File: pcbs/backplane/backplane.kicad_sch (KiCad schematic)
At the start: 65 parts

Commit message: Schematic file fix, misc. PCB
Fixed issue with KiCAD's automatic V5→V6 migration (corrected in 6.0.11) that caused problems with component references in multi-channel schematic sheets
Finished migration in amp ctrl PCB, inc. re-assigning "exclude from BOM" attributes to testpoints, solder jumpers
Added mounting hole to amp ctrl PCB for addl support to Ethernet jacks, power connector through stiffener
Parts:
- C10, C2, C20, C3, C61, C62: renamed from ?; value 100nF 50V X7R -> (none); footprint Capacitor_SMD:C_0603_1608Metric -> (none)
- C16, C17, C18, C19: renamed from ?; value 1uF 50V X7R -> (none); footprint Capacitor_SMD:C_0805_2012Metric -> (none)
- J10, J11, J9: renamed from ?; value AFBR-2624Z -> (none); footprint Martinos:AFBR-xx2xZ -> (none)
- J12: renamed from ?; value AFBR-1624Z -> (none); footprint Martinos:AFBR-xx2xZ -> (none)
- J17, J22, J27, J32, J37, J42, J47, J8: renamed from ?; value Conn_01x02 -> (none); footprint Martinos:Connector_Phoenix_1792229 -> (none)
- R10, R11, R3, R4: renamed from ?; value 1 -> (none); footprint Resistor_SMD:R_0805_2012Metric -> (none)
- R12: renamed from ?; value 560 -> (none); footprint Resistor_SMD:R_0805_2012Metric -> (none)
- R5: renamed from ?; value 10 0.25W -> (none); footprint Resistor_SMD:R_2010_5025Metric -> (none)
- R6, R7: renamed from ?; value 1 -> (none); footprint Resistor_SMD:R_1206_3216Metric -> (none)
- R8: renamed from ?; value 15K -> (none); footprint Resistor_SMD:R_0805_2012Metric -> (none)
- R9: renamed from ?; value 1K -> (none); footprint Resistor_SMD:R_0805_2012Metric -> (none)
- TP1, TP2, TP3, TP5: renamed from ?; value TestPoint_Flag -> (none); footprint TestPoint:TestPoint_Keystone_5019_Minature -> (none)
- gave numbers to parts that had none: 29

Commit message: Amp ctrl: lengthened ADC & DAC reset delay to ~50 ms (#14) Backplane: added clock multiplier for 10 Mhz scanner clock (fixes #21) Backplane: reduced R5 from 10 to 1 ohm, to avoid excessive voltage drop (#20) Backplane: replaced 15V regulator with efficient voltage limiter (#20) Backplane: changed all mounting holes to signal ground Backplane: replaced +2.5V regulator with a higher-current model to support FPGA I/O bank current draw Updated to KiCAD 8
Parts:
- C10, C2, C20, C3, C61, C62: value (none) -> 100nF 50V X7R; footprint (none) -> Capacitor_SMD:C_0603_1608Metric
- C16, C17, C18, C19: value (none) -> 1uF 50V X7R; footprint (none) -> Capacitor_SMD:C_0805_2012Metric
- J10, J11, J9: value (none) -> AFBR-2624Z; footprint (none) -> Martinos:AFBR-xx2xZ
- J12: value (none) -> AFBR-1624Z; footprint (none) -> Martinos:AFBR-xx2xZ
- J17, J22, J27, J32, J37, J42, J47, J8: value (none) -> Conn_01x02; footprint (none) -> Martinos:Connector_Phoenix_1792229
- R10, R11, R3, R4: value (none) -> 1; footprint (none) -> Resistor_SMD:R_0805_2012Metric
- R12: value (none) -> 560; footprint (none) -> Resistor_SMD:R_0805_2012Metric
- R5: value (none) -> 1 0.25W; footprint (none) -> Resistor_SMD:R_2010_5025Metric; Part Number RK73H2HTTE10R0F -> RK73H2HTTE1R00F
- R6, R7: value (none) -> 1; footprint (none) -> Resistor_SMD:R_1206_3216Metric
- R8: value (none) -> 15K; footprint (none) -> Resistor_SMD:R_0805_2012Metric
- R9: value (none) -> 1K; footprint (none) -> Resistor_SMD:R_0805_2012Metric
- TP1, TP2, TP3, TP5: value (none) -> TestPoint_Flag; footprint (none) -> TestPoint:TestPoint_Keystone_5019_Minature
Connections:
- net GND: now also H11.1, H14.1, H16.1, H17.1, H18.1, H19.1, H20.1, H5.1, H7.1, H9.1
- net GNDPWR: no longer H11.1, H14.1, H16.1, H17.1, H18.1, H19.1, H20.1, H5.1, H7.1, H9.1

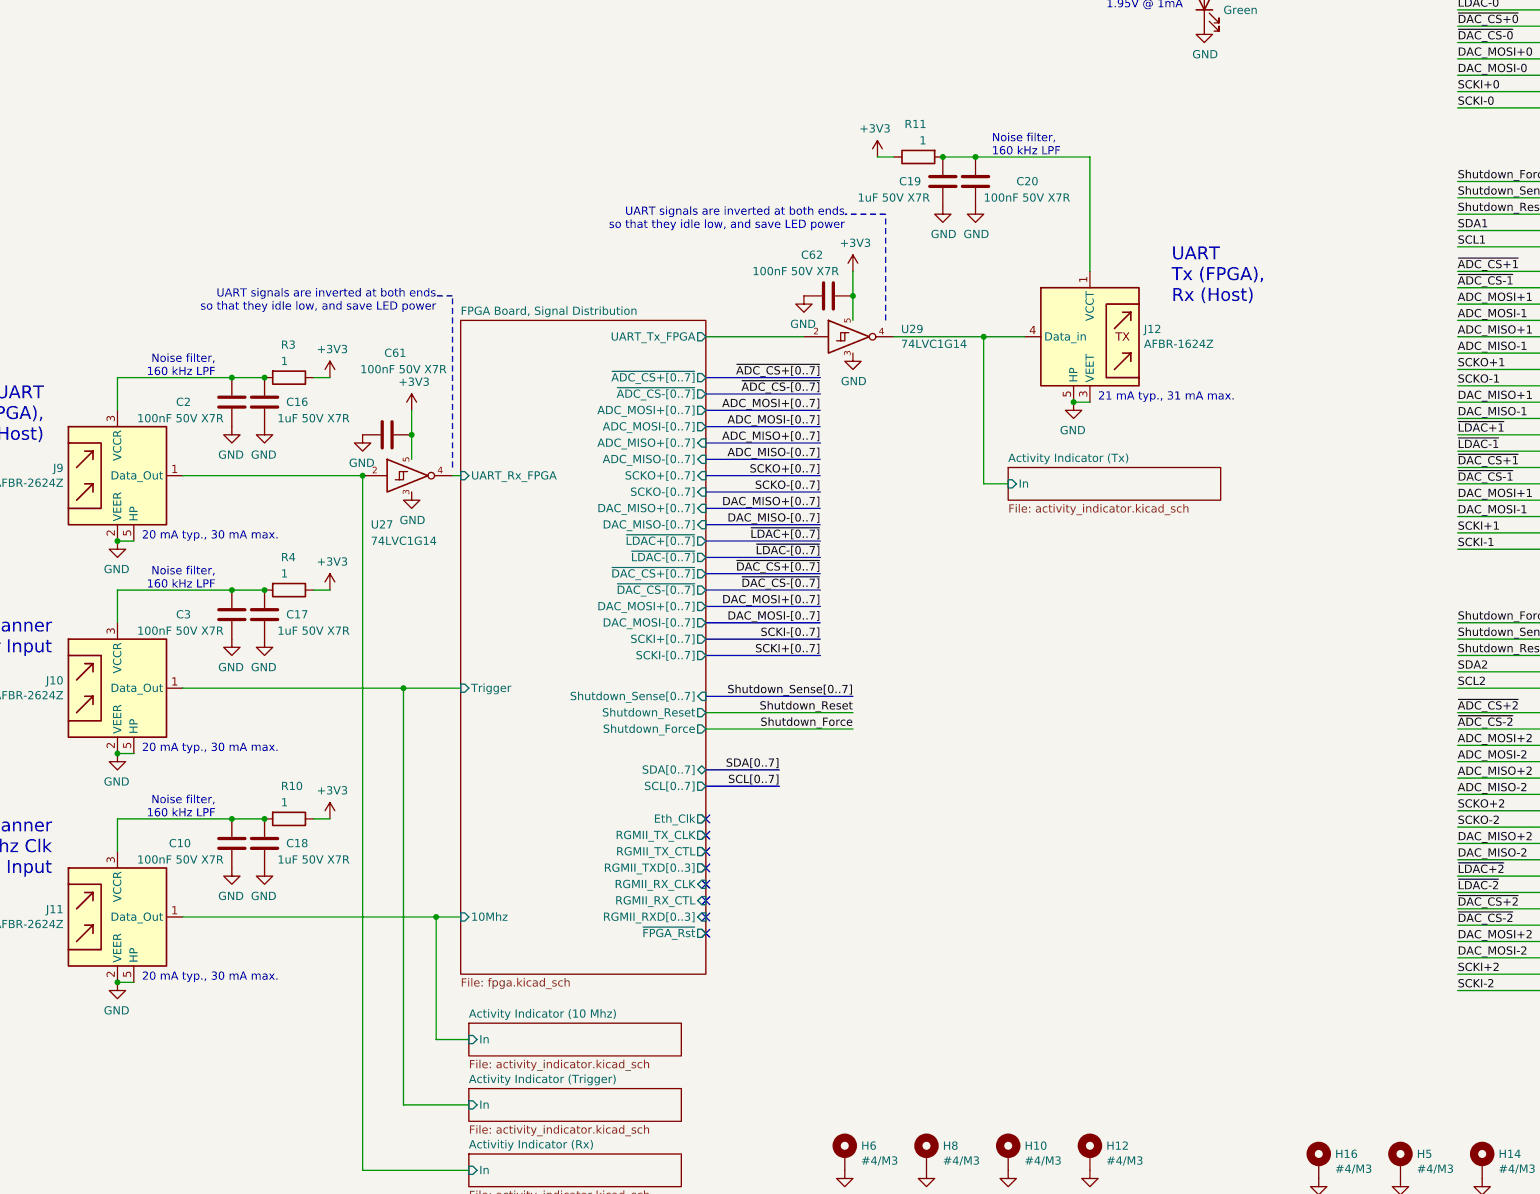
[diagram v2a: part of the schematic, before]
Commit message: Comms fix, misc. improvements
Added 33KΩ pull-ups & pull-downs to amp ctrl board's LVDS inputs, to solve issues caused by unconfigured FPGA pins during boot (fixes #23)
Swapped backplane power input polarity for consistency with power connectors (fixes #20)
Added "manual enable" optical input to backplane, for safety: requires positive enable to keep amplifiers enabled
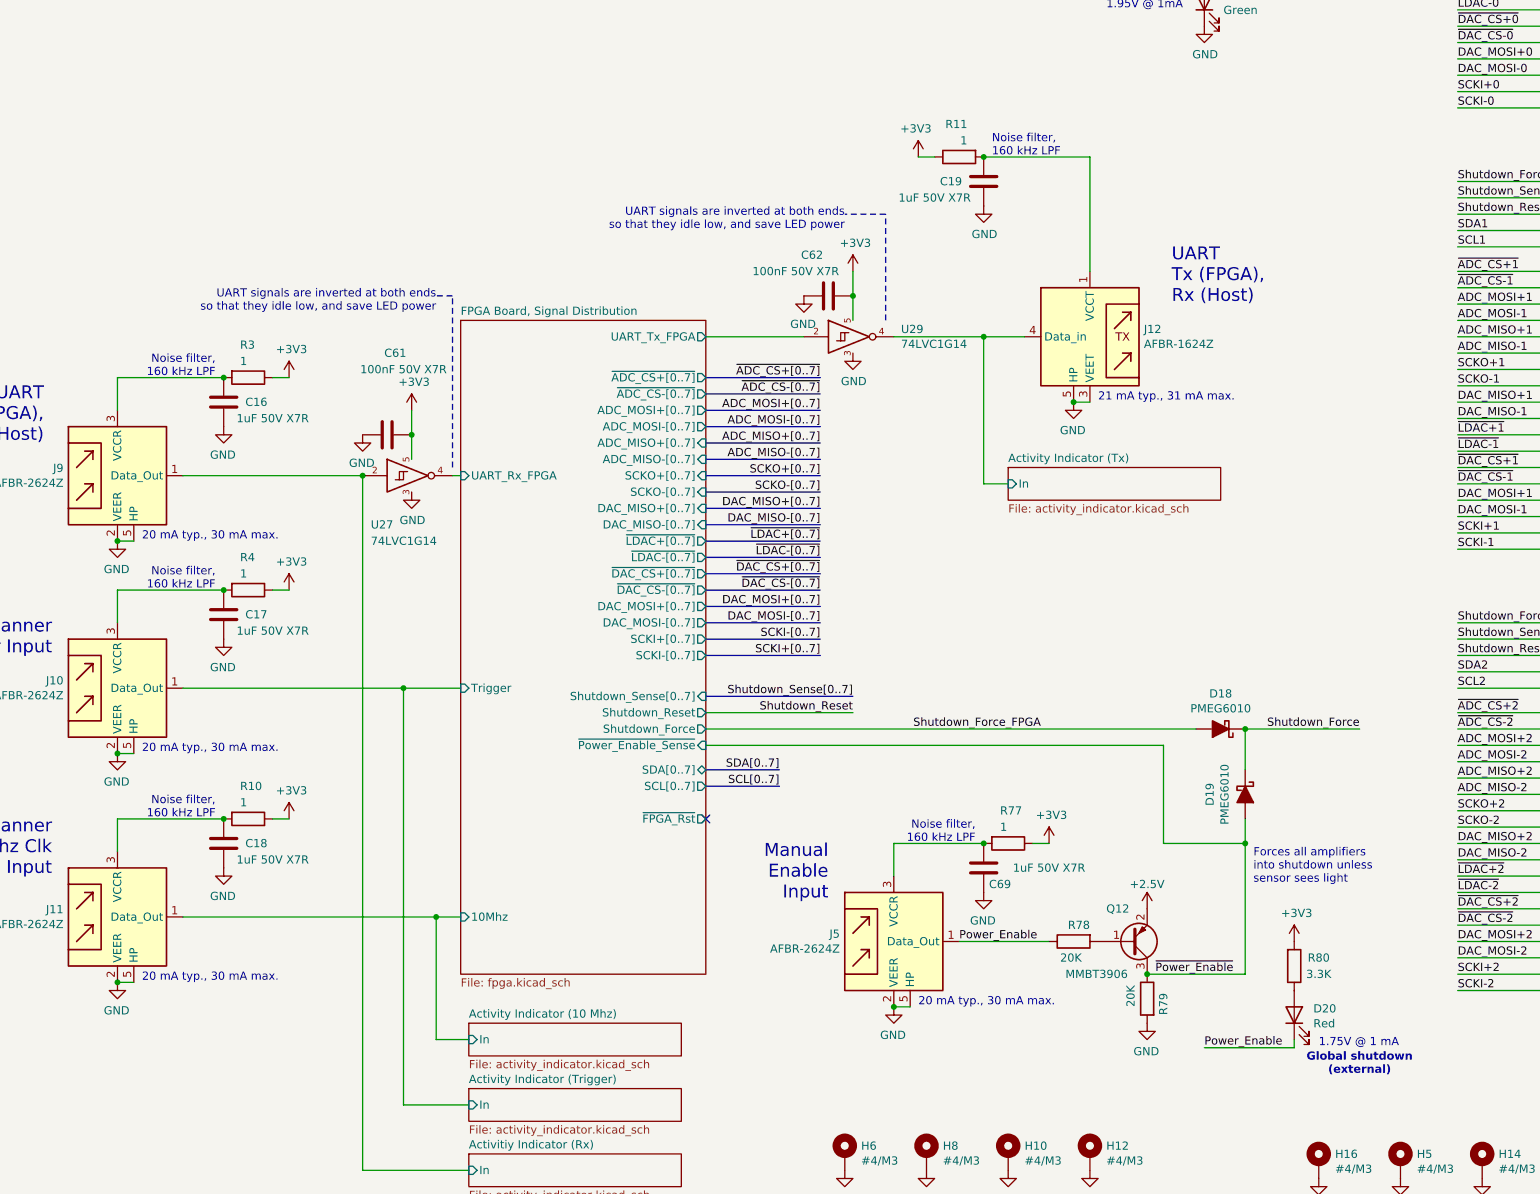
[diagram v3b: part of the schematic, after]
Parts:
- removed C10, C2, C20, C3: 100nF 50V X7R, Capacitor_SMD:C_0603_1608Metric, symbol Device:C
- added C69: 1uF 50V X7R, Capacitor_SMD:C_0805_2012Metric, symbol Device:C
- added D18, D19: PMEG6010, Diode_SMD:D_SOD-123F, symbol backplane-rescue:D_Schottky_ALT-Device
- added D20: Red, LED_SMD:LED_0805_2012Metric, symbol Device:LED
- added J5: AFBR-2624Z, Don:AFBR-xx2xZ, symbol Fiber_Optic:AFBR-2624Z
- added Q12: MMBT3906, Package_TO_SOT_SMD:SOT-23, symbol Transistor_BJT:MMBT3906
- added R77: 1, Resistor_SMD:R_0805_2012Metric, symbol Device:R
- added R78, R79: 20K, Resistor_SMD:R_0805_2012Metric, symbol Device:R
- added R80: 3.3K, Resistor_SMD:R_0805_2012Metric, symbol Device:R
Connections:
- net +2.5V: now also Q12.2 (E)
- net +3V3: now also R77.1, R80.2
- net GND: now also C69.1, J5.2 (VEER), J5.5 (HP), J5.8 (HP), R79.2
- net Shutdown_Force: now also D18.1 (K), D19.1 (K)
- new net: D20.2 (A), R80.1
- new net: Q12.1 (B), R78.2
- new net: C69.2, J5.3 (VCCR), R77.2
- new net Power_Enable: D20.1 (K), J5.1 (Data_Out), R78.1
- new net Shutdown_Force_FPGA: D18.2 (A)
- new net ~{Power_Enable}: D19.2 (A), Q12.3 (C), R79.1
- no-connect marks 8 -> 1
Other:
- sheet FPGA Board, Signal Distribution ports: added ~{Power_Enable_Sense}; removed Eth_Clk, RGMII_RXD[0..3], RGMII_RX_CLK, RGMII_RX_CTL, RGMII_TXD[0..3], RGMII_TX_CLK, RGMII_TX_CTL
- note added: "1.75V @ 1 mA"
- note added: "Forces all amplifiers into shutdown unless sensor sees light"
- note added: "Global shutdown (external)"
- note added: "Manual Enable Input"
- moved on the sheet: C16, C17, C18, C19, R10, R11, R3, R4

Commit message: Corrected power-up behavior
Backplane: Inverted polarity of Shutdown_Force (now Power_Enable_FPGA), to keep amps powered off until software starts: fixes #23
Backplane: Routed Shutdown_Force to unused pin 3 on RJ45 jack B to amp boards: fixes #23
Backplane: Added pull-up and pull-down resistors to fanout buffer inputs, to keep SCK & ~LDAC signals in proper state during power-on: fixes #23
Amp control: Added transistor to reset DAC & ADC from pin 3 of RJ45 jack B
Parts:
- removed Q12: MMBT3906, Package_TO_SOT_SMD:SOT-23, symbol Transistor_BJT:MMBT3906
- added C31, C34: 1uF 50V X7R, Capacitor_SMD:C_0805_2012Metric, symbol Device:C
- added D21: Red, LED_SMD:LED_0805_2012Metric, symbol Device:LED
- added D22: PMEG6010, Diode_SMD:D_SOD-123F, symbol backplane-rescue:D_Schottky_ALT-Device
- added L1: 500nH, Don:L_Coilcraft_2929SQ-501, symbol Device:L
- added Q12: MMBT3904, Package_TO_SOT_SMD:SOT-23, symbol Transistor_BJT:MMBT3904
- added R18: 1 0.25W, Resistor_SMD:R_2010_5025Metric, symbol Device:R
- added R81, R88: 20K, Resistor_SMD:R_0805_2012Metric, symbol Device:R
- added R82, R83: 3.3K, Resistor_SMD:R_0805_2012Metric, symbol Device:R
- added R89: 10K, Resistor_SMD:R_0805_2012Metric, symbol Device:R
- J10, J11, J12, J9: footprint Martinos:AFBR-xx2xZ -> Don:AFBR-xx2xZ
- J17, J22, J27, J32, J37, J42, J47, J8: footprint Martinos:Connector_Phoenix_1792229 -> Don:Connector_Phoenix_1792229
- R79: value 20K -> 3.3K; Part Number RK73H2ATTD1001F -> RK73H2ATTD3301F
- U27, U29: footprint Martinos_std:SOT-23-5 -> Don_std:SOT-23-5
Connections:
- net +3V3: now also R79.2, R81.1
- net GND: now also C31.1, C34.1, Q12.2 (E), R82.1, R83.1, R88.1; no longer R79.2
- net Shutdown_Force: now also R78.2, Q12.3 (C); no longer D18.1 (K), D19.1 (K)
- net Shutdown_Force_FPGA: now also D18.1 (K), D21.1 (K), R82.2; no longer D18.2 (A)
- net VD: now also R78.1, C34.2, L1.2; no longer C4.1, F1.1, TP5.1
- net Power_Enable renamed Power_Enable_Ext
- net Power_Enable_Ext: now also D19.1 (K), R83.2, R89.1; no longer R78.1
- net ~{Power_Enable}: no longer names the net of D19.2 (A)
- net ~{Power_Enable}: now also D18.2 (A), D22.2 (A), R81.2; no longer R79.1
- new net: C31.2, C4.1, F1.1, R18.2, TP5.1
- new net: L1.1, R18.1
- new net: D22.1 (K), Q12.1 (B)
- new net: D21.2 (A), R79.1
- new net FPGA Board, Signal Distribution/Power_Enable_Ext_Sense: R88.2, R89.2
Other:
- sheet FPGA Board, Signal Distribution ports: added Power_Enable_Ext_Sense, Power_Enable_FPGA; removed Shutdown_Force, ~{Power_Enable_Sense}
- note added: "22 mW @ 150 mA"
- note added: "Global shutdown (FPGA)"
- note added: "Noise filter, 225 kHz LPF"
- note added: "Translates from 3.3V receiver logic level to 2.5V FPGA logic level"
- moved on the sheet: C19, C69, D18, D19, D20, D3, D5, J5, R11, R12, R77, R78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

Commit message: Misc. cleanup for mfg & improvements
Minor backplane pinout doc corrections (SCKO5 polarity, clarified some descriptions)
Backplane: Added differential- and common-mode (to standoffs) power filtering, for EMI escaping over power wiring
Amp ctrl: Changed DAC testpoints from individual pads to Keystone 5019 for easier probing
Corrected part numbers, DNP vs. non-BOM-item indications, other misc. BOM issues
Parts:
- added C10, C2, C20, C3, C68, C70, C71, C72, C73, C74, C75: 100nF 50V X7R, Capacitor_SMD:C_0603_1608Metric, symbol Device:C
- F1, J1, R6, R7: now not fitted
- H1, H10, H11, H12, H13, H14, H15, H16, H17, H18, H19, H2, H20, H3, H4, H5, H6, H7, H8, H9: now left out of the parts list
- R78, R81, R88: Part Number RK73H2ATTD1001F -> RK73H2ATTD2002F
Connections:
- net +VDC: now also C10.1, C2.1, C20.1, C3.1, C68.1, C70.1, C71.1, C72.1
- net GND: now also C73.2, C74.2, C75.2
- net GNDPWR: now also C10.2, C2.2, C20.2, C3.2, C68.2, C70.2, C71.2, C72.2, C73.1, C74.1, C75.1
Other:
- moved on the sheet: J17, J22, J27, J32, J37, J42, J47, J8

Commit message: Backplane cleanup for mfg, schematic clarifications, added alt. power connectors
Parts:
- added J14, J19, J24, J29, J34, J39, J44, J48: Conn_01x02, Don:Connector_Phoenix_1190363, symbol Connector_Generic:Conn_01x02
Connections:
- net +VDC: now also J14.2 (Pin_2), J19.2 (Pin_2), J24.2 (Pin_2), J29.2 (Pin_2), J34.2 (Pin_2), J39.2 (Pin_2), J44.2 (Pin_2), J48.2 (Pin_2)
- net GNDPWR: now also J14.1 (Pin_1), J19.1 (Pin_1), J24.1 (Pin_1), J29.1 (Pin_1), J34.1 (Pin_1), J39.1 (Pin_1), J44.1 (Pin_1), J48.1 (Pin_1)
- net Shutdown_Force_FPGA renamed Power_Enable_FPGA
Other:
- note added: "Mounting holes"
- note added: "Power connections to amp boards"
- note removed: "Forces all amplifiers into shutdown unless sensor sees light"
- note removed: "Translates from 3.3V receiver logic level to 2.5V FPGA logic level"
- moved on the sheet: C10, C16, C17, C18, C19, C2, C20, C3, C61, C62, C68, C69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

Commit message: Moved all project-specific symbols & footprints into new "shim" libraries Updated projects to reference the new "shim" library
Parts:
- J10, J11, J12, J5, J9: footprint Don:AFBR-xx2xZ -> shim:AFBR-xx2xZ
- J14, J19, J24, J29, J34, J39, J44, J48: footprint Don:Connector_Phoenix_1190363 -> shim:Connector_Phoenix_1190363
- J17, J22, J27, J32, J37, J42, J47, J8: footprint Don:Connector_Phoenix_1792229 -> shim:Connector_Phoenix_1792229
- L1: footprint Don:L_Coilcraft_2929SQ-501 -> shim:L_Coilcraft_2929SQ-501
- U27, U29: footprint Don_std:SOT-23-5 -> Package_TO_SOT_SMD:SOT-23-5
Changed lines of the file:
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@@
 			)
 		)
-		(property "Footprint" "Don:Connector_Phoenix_1792229"
+		(property "Footprint" "shim:Connector_Phoenix_1792229"
 			(at 422.91 320.04 0)
 			(effects
@@
 			)
 		)
-		(property "Footprint" "Don:Connector_Phoenix_1792229"
+		(property "Footprint" "shim:Connector_Phoenix_1792229"
 			(at 434.34 320.04 0)
 			(effects
@@
 			)
 		)
-		(property "Footprint" "Don:Connector_Phoenix_1792229"
+		(property "Footprint" "shim:Connector_Phoenix_1792229"
 			(at 422.91 341.63 0)
 			(effects
@@
 			)
 		)
-		(property "Footprint" "Don:Connector_Phoenix_1792229"
+		(property "Footprint" "shim:Connector_Phoenix_1792229"
 			(at 434.34 341.63 0)
 			(effects
@@
 			)
 		)
-		(property "Footprint" "Don:Connector_Phoenix_1792229"
+		(property "Footprint" "shim:Connector_Phoenix_1792229"
 			(at 445.77 320.04 0)
 			(effects
@@
 			)
 		)
-		(property "Footprint" "Don:Connector_Phoenix_1792229"
+		(property "Footprint" "shim:Connector_Phoenix_1792229"
 			(at 445.77 341.63 0)
 			(effects
@@
 			)
 		)
-		(property "Footprint" "Don:Connector_Phoenix_1792229"
+		(property "Footprint" "shim:Connector_Phoenix_1792229"
 			(at 457.2 320.04 0)
 			(effects
@@
 			)
 		)
-		(property "Footprint" "Don:Connector_Phoenix_1792229"
+		(property "Footprint" "shim:Connector_Phoenix_1792229"
 			(at 457.2 341.63 0)
 			(effects
@@
 			)
 		)
-		(property "Footprint" "Don:AFBR-xx2xZ"
+		(property "Footprint" "shim:AFBR-xx2xZ"
 			(at 210.82 152.4 0)
 			(effects
@@
 			)
 		)
-		(property "Footprint" "Don:AFBR-xx2xZ"
+		(property "Footprint" "shim:AFBR-xx2xZ"
 			(at 57.15 171.45 0)
 			(effects
@@
 			)
 		)
-		(property "Footprint" "Don:AFBR-xx2xZ"
+		(property "Footprint" "shim:AFBR-xx2xZ"
 			(at 57.15 204.47 0)
 			(effects
@@
 			)
 		)
-		(property "Footprint" "Don:AFBR-xx2xZ"
+		(property "Footprint" "shim:AFBR-xx2xZ"
 			(at 57.15 240.03 0)
 			(effects
@@
 			)
 		)
-		(property "Footprint" "Don_std:SOT-23-5"
+		(property "Footprint" "Package_TO_SOT_SMD:SOT-23-5"
 			(at 173.99 137.16 0)
 			(effects
@@
 			)
 		)
-		(property "Footprint" "Don_std:SOT-23-5"
+		(property "Footprint" "Package_TO_SOT_SMD:SOT-23-5"
 			(at 105.41 158.75 0)
 			(effects
@@
 			)
 		)
-		(property "Footprint" "Don:Connector_Phoenix_1190363"
+		(property "Footprint" "shim:Connector_Phoenix_1190363"
 			(at 510.54 342.9 0)
 			(effects
@@
 			)
 		)
-		(property "Footprint" "Don:L_Coilcraft_2929SQ-501"
+		(property "Footprint" "shim:L_Coilcraft_2929SQ-501"
 			(at 207.01 26.67 0)
 			(effects
@@
 			)
 		)
-		(property "Footprint" "Don:Connector_Phoenix_1190363"
+		(property "Footprint" "shim:Connector_Phoenix_1190363"
 			(at 496.57 342.9 0)
 			(effects
@@
 			)
 		)
-		(property "Footprint" "Don:Connector_Phoenix_1190363"
+		(property "Footprint" "shim:Connector_Phoenix_1190363"
 			(at 510.54 318.77 0)
 			(effects
@@
 			)
 		)
-		(property "Footprint" "Don:Connector_Phoenix_1190363"
+		(property "Footprint" "shim:Connector_Phoenix_1190363"
 			(at 524.51 342.9 0)
 			(effects
@@
 			)
 		)
-		(property "Footprint" "Don:Connector_Phoenix_1190363"
+		(property "Footprint" "shim:Connector_Phoenix_1190363"
 			(at 482.6 318.77 0)
 			(effects
@@
 			)
 		)
-		(property "Footprint" "Don:Connector_Phoenix_1190363"
+		(property "Footprint" "shim:Connector_Phoenix_1190363"
 			(at 482.6 342.9 0)
 			(effects
@@
 			)
 		)
-		(property "Footprint" "Don:Connector_Phoenix_1190363"
+		(property "Footprint" "shim:Connector_Phoenix_1190363"
 			(at 496.57 318.77 0)
 			(effects
@@
 			)
 		)
-		(property "Footprint" "Don:Connector_Phoenix_1190363"
+		(property "Footprint" "shim:Connector_Phoenix_1190363"
 			(at 524.51 318.77 0)
 			(effects
@@
 			)
 		)
-		(property "Footprint" "Don:AFBR-xx2xZ"
+		(property "Footprint" "shim:AFBR-xx2xZ"
 			(at 177.8 297.18 0)
 			(effects
